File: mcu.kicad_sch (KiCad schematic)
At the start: 16 parts, among them J10 Conn_PIC_ICSP_ICD, U10 PIC18F24K42, U11 LM4040DBZ-2.0

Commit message: WIP routing
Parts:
- C301: renamed from C10; value 100n -> (none); footprint Capacitor_SMD:C_0402_1005Metric -> (none)
- J301: renamed from J10; value Conn_PIC_ICSP_ICD -> (none); footprint Connector_PinHeader_2.54mm:PinHeader_1x06_P2.54mm_Vertical -> (none)
- JP301: renamed from JP10; value SB -> (none); footprint Jumper:SolderJumper-2_P1.3mm_Open_TrianglePad1.0x1.5mm -> (none)
- JP302: renamed from JP11; value SB -> (none); footprint Jumper:SolderJumper-2_P1.3mm_Open_TrianglePad1.0x1.5mm -> (none)
- JP303: renamed from JP12; value SB -> (none); footprint Jumper:SolderJumper-2_P1.3mm_Open_TrianglePad1.0x1.5mm -> (none)
- JP304: renamed from JP13; value SB -> (none); footprint Jumper:SolderJumper-2_P1.3mm_Open_TrianglePad1.0x1.5mm -> (none)
- R301: renamed from R10; value 10k -> (none); footprint Resistor_SMD:R_0805_2012Metric -> (none)
- R302: renamed from R14; value 10k -> (none); footprint Resistor_SMD:R_0805_2012Metric -> (none)
- R303: renamed from R15; value 10k -> (none); footprint Resistor_SMD:R_0805_2012Metric -> (none)
- R304: renamed from R16; value 10k -> (none); footprint Resistor_SMD:R_0805_2012Metric -> (none)
- R305: renamed from R17; value 4.7k -> (none); footprint Resistor_SMD:R_0805_2012Metric -> (none)
- R306: renamed from R13; value 10k -> (none); footprint Resistor_SMD:R_0805_2012Metric -> (none)
- R307: renamed from R11; value 4.7k -> (none); footprint Resistor_SMD:R_0805_2012Metric -> (none)
- R308: renamed from R12; value 4.7k -> (none); footprint Resistor_SMD:R_0805_2012Metric -> (none)
- U301: renamed from U11; value LM4040DBZ-2.0 -> (none); footprint Package_TO_SOT_SMD:SOT-23 -> (none)
- U302: renamed from U10; value PIC18F24K42 -> (none); footprint Package_SO:SSOP-28_5.3x10.2mm_P0.65mm -> (none)
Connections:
- net ICSPCLK is gone; now on net 3V3_sense: J301.5 (PGC/ICSPCLK), U302.27 (ICSPCLK/CLCIN2/CTS2/ANB6/RB6)
- net ICSPDAT is gone; now on net 5V_sense: J301.4 (PGD/ICSPDAT), U302.28 (ICSPDAT/CLCIN3/RX2/DAC1OUT2/ANB7/RB7)
- net 3V3_sense: no longer U302.16 (ANC5/RC5)
- net 5V_sense: no longer U302.17 (CTS1/ANC6/RC6)
- net current_measure: now also U302.16 (ANC5/RC5); no longer U302.25 (ANB4/RB4)
- net pwm_ctrl: now also U302.17 (CTS1/ANC6/RC6); no longer U302.26 (ANB5/RB5)
- net range.100ma: now also U302.25 (ANB4/RB4); no longer U302.24 (C2IN2-/C1IN2-/ANB3/RB3)
- net range.10a: now also U302.26 (ANB5/RB5)
- net range.1ma: now also U302.24 (C2IN2-/C1IN2-/ANB3/RB3)
- net load_voltage: now reaches U302.2 (RA0/ANA0/C1IN0-/C2IN0-/CLCIN0)
- net temp_sense: now reaches U302.3 (RA1/ANA1/C1IN1-/C2IN1-/CLCIN1)
- net temp_en: now reaches U302.4 (RA2/Vref-/ANA2/DAC1OUT1/C1IN0+/C2IN0+)

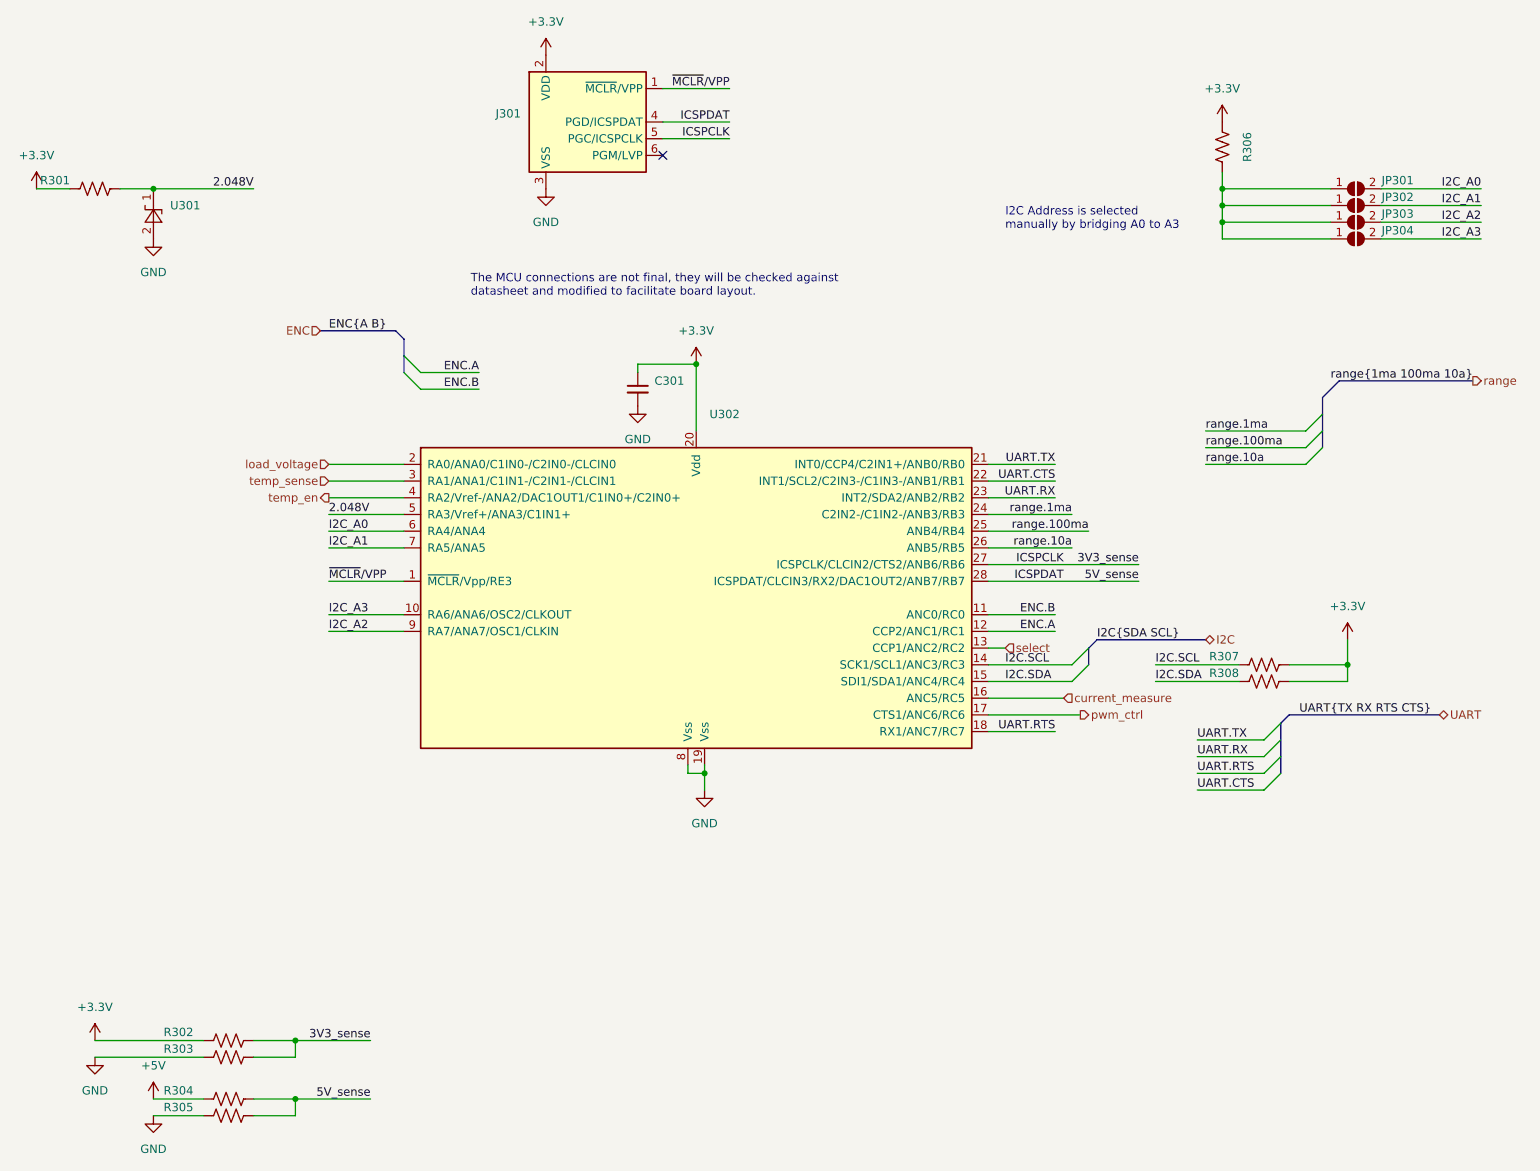
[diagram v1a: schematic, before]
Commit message: Fix and tune differential pair and zones
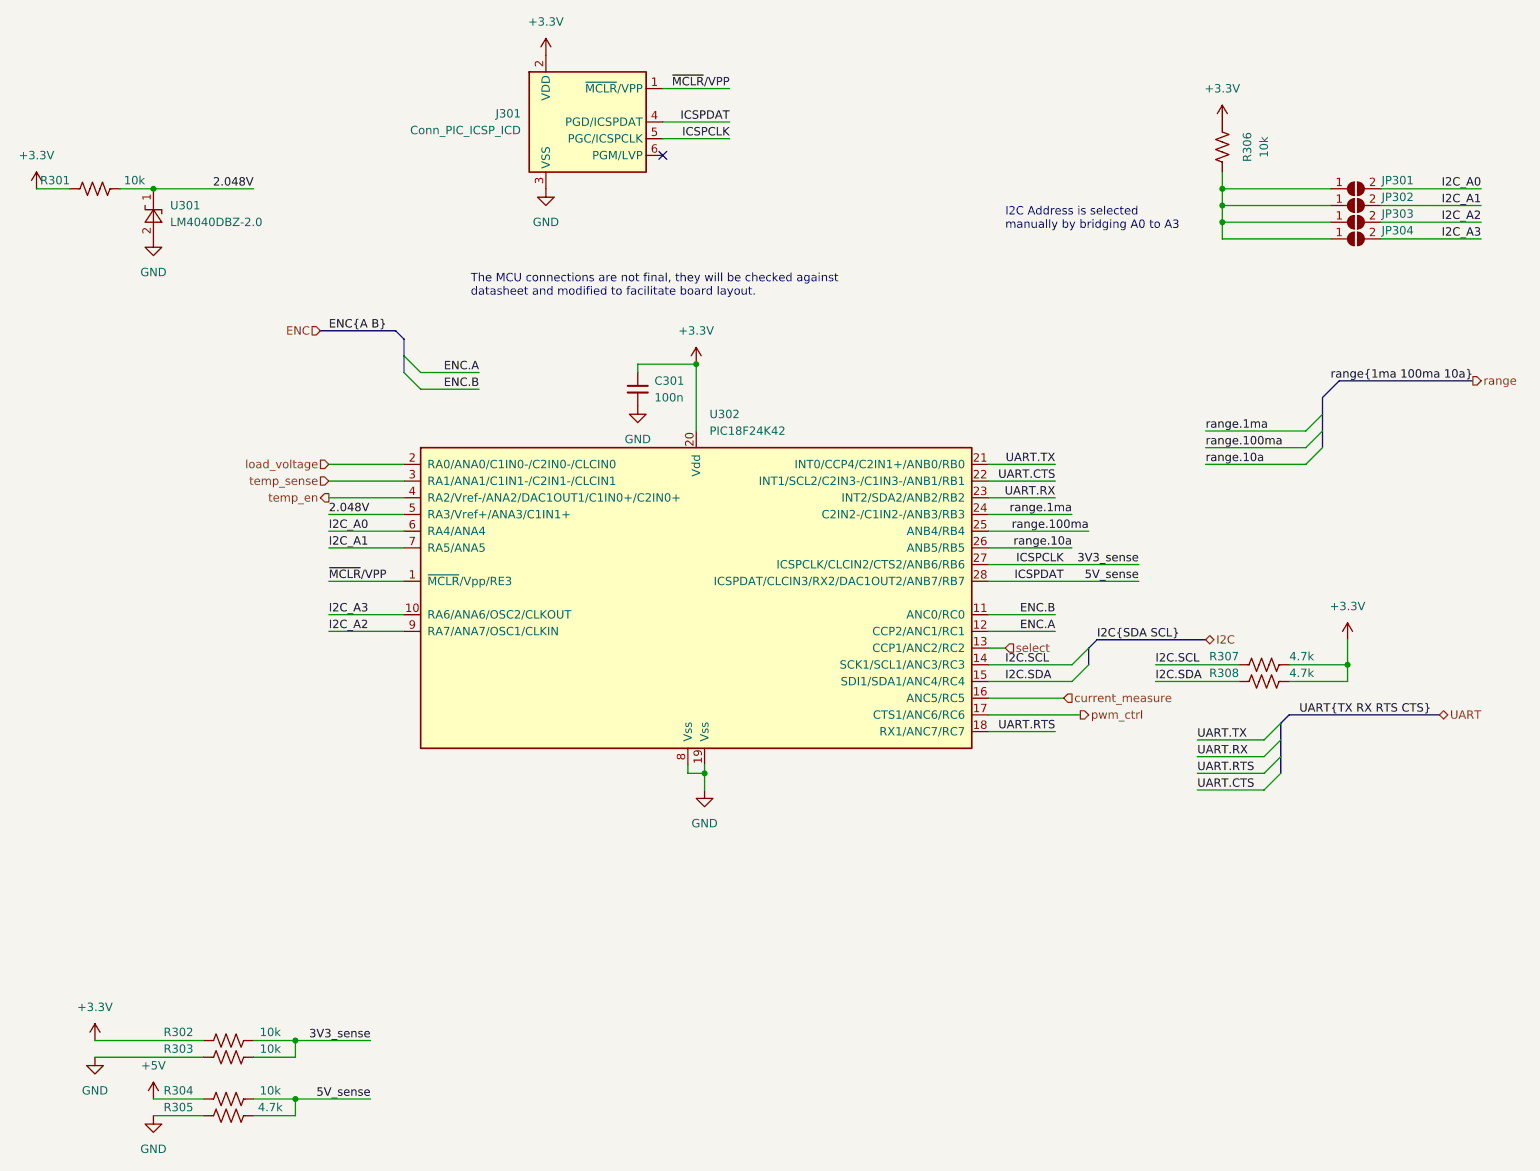
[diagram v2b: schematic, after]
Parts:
- C301: value (none) -> 100n; footprint (none) -> Capacitor_SMD:C_0402_1005Metric
- J301: value (none) -> Conn_PIC_ICSP_ICD; footprint (none) -> Connector_PinHeader_2.54mm:PinHeader_1x06_P2.54mm_Vertical
- JP301, JP302, JP303, JP304: value (none) -> SB; footprint (none) -> Jumper:SolderJumper-2_P1.3mm_Open_TrianglePad1.0x1.5mm
- R301, R302, R303, R304, R306: value (none) -> 10k; footprint (none) -> Resistor_SMD:R_0805_2012Metric
- R305, R307, R308: value (none) -> 4.7k; footprint (none) -> Resistor_SMD:R_0805_2012Metric
- U301: value (none) -> LM4040DBZ-2.0; footprint (none) -> Package_TO_SOT_SMD:SOT-23
- U302: value (none) -> PIC18F24K42; footprint (none) -> Package_SO:SSOP-28_5.3x10.2mm_P0.65mm
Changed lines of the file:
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@@
       (effects (font (size 1.27 1.27)) (justify right))
     )
-    (property "Value" "" (id 1) (at 236.22 114.3 90)
-      (effects (font (size 1.27 1.27)) (justify right))
-    )
-    (property "Footprint" "" (id 2) (at 228.346 116.586 90)
+    (property "Value" "4.7k" (id 1) (at 236.22 114.3 90)
+      (effects (font (size 1.27 1.27)) (justify right))
+    )
+    (property "Footprint" "Resistor_SMD:R_0805_2012Metric" (id 2) (at 228.346 116.586 90)
       (effects (font (size 1.27 1.27)) hide)
     )
@@
       (effects (font (size 1.27 1.27)) (justify right))
     )
-    (property "Value" "" (id 1) (at 58.42 39.37 90)
-      (effects (font (size 1.27 1.27)) (justify right))
-    )
-    (property "Footprint" "" (id 2) (at 50.546 41.656 90)
+    (property "Value" "10k" (id 1) (at 58.42 39.37 90)
+      (effects (font (size 1.27 1.27)) (justify right))
+    )
+    (property "Footprint" "Resistor_SMD:R_0805_2012Metric" (id 2) (at 50.546 41.656 90)
       (effects (font (size 1.27 1.27)) hide)
     )
@@
       (effects (font (size 1.27 1.27)) (justify right))
     )
-    (property "Value" "" (id 1) (at 115.57 31.7499 0)
-      (effects (font (size 1.27 1.27)) (justify right))
-    )
-    (property "Footprint" "" (id 2) (at 125.73 26.67 0)
+    (property "Value" "Conn_PIC_ICSP_ICD" (id 1) (at 115.57 31.7499 0)
+      (effects (font (size 1.27 1.27)) (justify right))
+    )
+    (property "Footprint" "Connector_PinHeader_2.54mm:PinHeader_1x06_P2.54mm_Vertical" (id 2) (at 125.73 26.67 0)
       (effects (font (size 1.27 1.27)) hide)
     )
@@
     (in_bom yes) (on_board yes)
     (property "Reference" "R302" (id 0) (at 63.5 168.91 90))
-    (property "Value" "" (id 1) (at 77.47 168.91 90))
-    (property "Footprint" "" (id 2) (at 70.866 171.196 90)
+    (property "Value" "10k" (id 1) (at 77.47 168.91 90))
+    (property "Footprint" "Resistor_SMD:R_0805_2012Metric" (id 2) (at 70.866 171.196 90)
       (effects (font (size 1.27 1.27)) hide)
     )
@@
     (in_bom yes) (on_board yes)
     (property "Reference" "JP301" (id 0) (at 248.92 39.37 0))
-    (property "Value" "" (id 1) (at 242.57 36.83 0)
-      (effects (font (size 1.27 1.27)) hide)
-    )
-    (property "Footprint" "" (id 2) (at 242.57 40.64 0)
+    (property "Value" "SB" (id 1) (at 242.57 36.83 0)
+      (effects (font (size 1.27 1.27)) hide)
+    )
+    (property "Footprint" "Jumper:SolderJumper-2_P1.3mm_Open_TrianglePad1.0x1.5mm" (id 2) (at 242.57 40.64 0)
       (effects (font (size 1.27 1.27)) hide)
     )
@@
     (in_bom yes) (on_board yes)
     (property "Reference" "R303" (id 0) (at 63.5 171.45 90))
-    (property "Value" "" (id 1) (at 77.47 171.45 90))
-    (property "Footprint" "" (id 2) (at 71.374 171.704 90)
+    (property "Value" "10k" (id 1) (at 77.47 171.45 90))
+    (property "Footprint" "Resistor_SMD:R_0805_2012Metric" (id 2) (at 71.374 171.704 90)
       (effects (font (size 1.27 1.27)) hide)
     )
@@
       (effects (font (size 1.27 1.27)) (justify left))
     )
-    (property "Value" "" (id 1) (at 144.2594 77.47 0)
+    (property "Value" "PIC18F24K42" (id 1) (at 144.2594 77.47 0)
       (effects (font (size 1.27 1.27)) (justify left))
     )
-    (property "Footprint" "" (id 2) (at 125.73 115.57 0)
+    (property "Footprint" "Package_SO:SSOP-28_5.3x10.2mm_P0.65mm" (id 2) (at 125.73 115.57 0)
       (effects (font (size 1.27 1.27)) hide)
     )
@@
     (in_bom yes) (on_board yes)
     (property "Reference" "R304" (id 0) (at 63.5 177.8 90))
-    (property "Value" "" (id 1) (at 77.47 177.8 90))
-    (property "Footprint" "" (id 2) (at 70.866 180.086 90)
+    (property "Value" "10k" (id 1) (at 77.47 177.8 90))
+    (property "Footprint" "Resistor_SMD:R_0805_2012Metric" (id 2) (at 70.866 180.086 90)
       (effects (font (size 1.27 1.27)) hide)
     )
@@
       (effects (font (size 1.27 1.27)) (justify right))
     )
-    (property "Value" "" (id 1) (at 62.23 45.7199 90)
-      (effects (font (size 1.27 1.27)) (justify right))
-    )
-    (property "Footprint" "" (id 2) (at 64.77 44.45 0)
+    (property "Value" "LM4040DBZ-2.0" (id 1) (at 62.23 45.7199 90)
+      (effects (font (size 1.27 1.27)) (justify right))
+    )
+    (property "Footprint" "Package_TO_SOT_SMD:SOT-23" (id 2) (at 64.77 44.45 0)
       (effects (font (size 1.27 1.27) italic) hide)
     )
@@
       (effects (font (size 1.27 1.27)) (justify left))
     )
-    (property "Value" "" (id 1) (at 135.89 72.3962 0)
+    (property "Value" "100n" (id 1) (at 135.89 72.3962 0)
       (effects (font (size 1.27 1.27)) (justify left))
     )
-    (property "Footprint" "" (id 2) (at 133.35 71.12 0)
+    (property "Footprint" "Capacitor_SMD:C_0402_1005Metric" (id 2) (at 133.35 71.12 0)
       (effects (font (size 1.27 1.27)) hide)
     )
@@
     (in_bom yes) (on_board yes)
     (property "Reference" "R306" (id 0) (at 226.06 34.29 90))
-    (property "Value" "" (id 1) (at 228.6 34.29 90))
-    (property "Footprint" "" (id 2) (at 221.234 34.036 90)
+    (property "Value" "10k" (id 1) (at 228.6 34.29 90))
+    (property "Footprint" "Resistor_SMD:R_0805_2012Metric" (id 2) (at 221.234 34.036 90)
       (effects (font (size 1.27 1.27)) hide)
     )
@@
       (effects (font (size 1.27 1.27)) (justify right))
     )
-    (property "Value" "" (id 1) (at 236.22 111.76 90)
-      (effects (font (size 1.27 1.27)) (justify right))
-    )
-    (property "Footprint" "" (id 2) (at 228.346 114.046 90)
+    (property "Value" "4.7k" (id 1) (at 236.22 111.76 90)
+      (effects (font (size 1.27 1.27)) (justify right))
+    )
+    (property "Footprint" "Resistor_SMD:R_0805_2012Metric" (id 2) (at 228.346 114.046 90)
       (effects (font (size 1.27 1.27)) hide)
     )
@@
     (in_bom yes) (on_board yes)
     (property "Reference" "JP303" (id 0) (at 248.92 44.45 0))
-    (property "Value" "" (id 1) (at 242.57 41.91 0)
-      (effects (font (size 1.27 1.27)) hide)
-    )
-    (property "Footprint" "" (id 2) (at 242.57 45.72 0)
+    (property "Value" "SB" (id 1) (at 242.57 41.91 0)
+      (effects (font (size 1.27 1.27)) hide)
+    )
+    (property "Footprint" "Jumper:SolderJumper-2_P1.3mm_Open_TrianglePad1.0x1.5mm" (id 2) (at 242.57 45.72 0)
       (effects (font (size 1.27 1.27)) hide)
     )
@@
     (in_bom yes) (on_board yes)
     (property "Reference" "JP304" (id 0) (at 248.92 46.99 0))
-    (property "Value" "" (id 1) (at 242.57 44.45 0)
-      (effects (font (size 1.27 1.27)) hide)
-    )
-    (property "Footprint" "" (id 2) (at 242.57 48.26 0)
+    (property "Value" "SB" (id 1) (at 242.57 44.45 0)
+      (effects (font (size 1.27 1.27)) hide)
+    )
+    (property "Footprint" "Jumper:SolderJumper-2_P1.3mm_Open_TrianglePad1.0x1.5mm" (id 2) (at 242.57 48.26 0)
       (effects (font (size 1.27 1.27)) hide)
     )
@@
     (in_bom yes) (on_board yes)
     (property "Reference" "JP302" (id 0) (at 248.92 41.91 0))
-    (property "Value" "" (id 1) (at 242.57 39.37 0)
-      (effects (font (size 1.27 1.27)) hide)
-    )
-    (property "Footprint" "" (id 2) (at 242.57 43.18 0)
+    (property "Value" "SB" (id 1) (at 242.57 39.37 0)
+      (effects (font (size 1.27 1.27)) hide)
+    )
+    (property "Footprint" "Jumper:SolderJumper-2_P1.3mm_Open_TrianglePad1.0x1.5mm" (id 2) (at 242.57 43.18 0)
       (effects (font (size 1.27 1.27)) hide)
     )
@@
     (in_bom yes) (on_board yes)
     (property "Reference" "R305" (id 0) (at 63.5 180.34 90))
-    (property "Value" "" (id 1) (at 77.47 180.34 90))
-    (property "Footprint" "" (id 2) (at 71.374 180.594 90)
-      (effects (font (size 1.27 1.27)) hide)
-    )
+    (property "Value" "4.7k" (id 1) (at 77.47 180.34 90))
+    (property "Footprint" "Resistor_SMD:R_0805_2012Metric" (id 2) (at 71.374 180.594 90)
+      (effects (font (size 1.27 1.27)) hide)
+    )
